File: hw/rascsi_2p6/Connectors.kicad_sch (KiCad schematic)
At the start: 3 parts, among them J20 171826-4, J3 Conn_02x25_Odd_Even, J9 Conn_02x25_Odd_Even

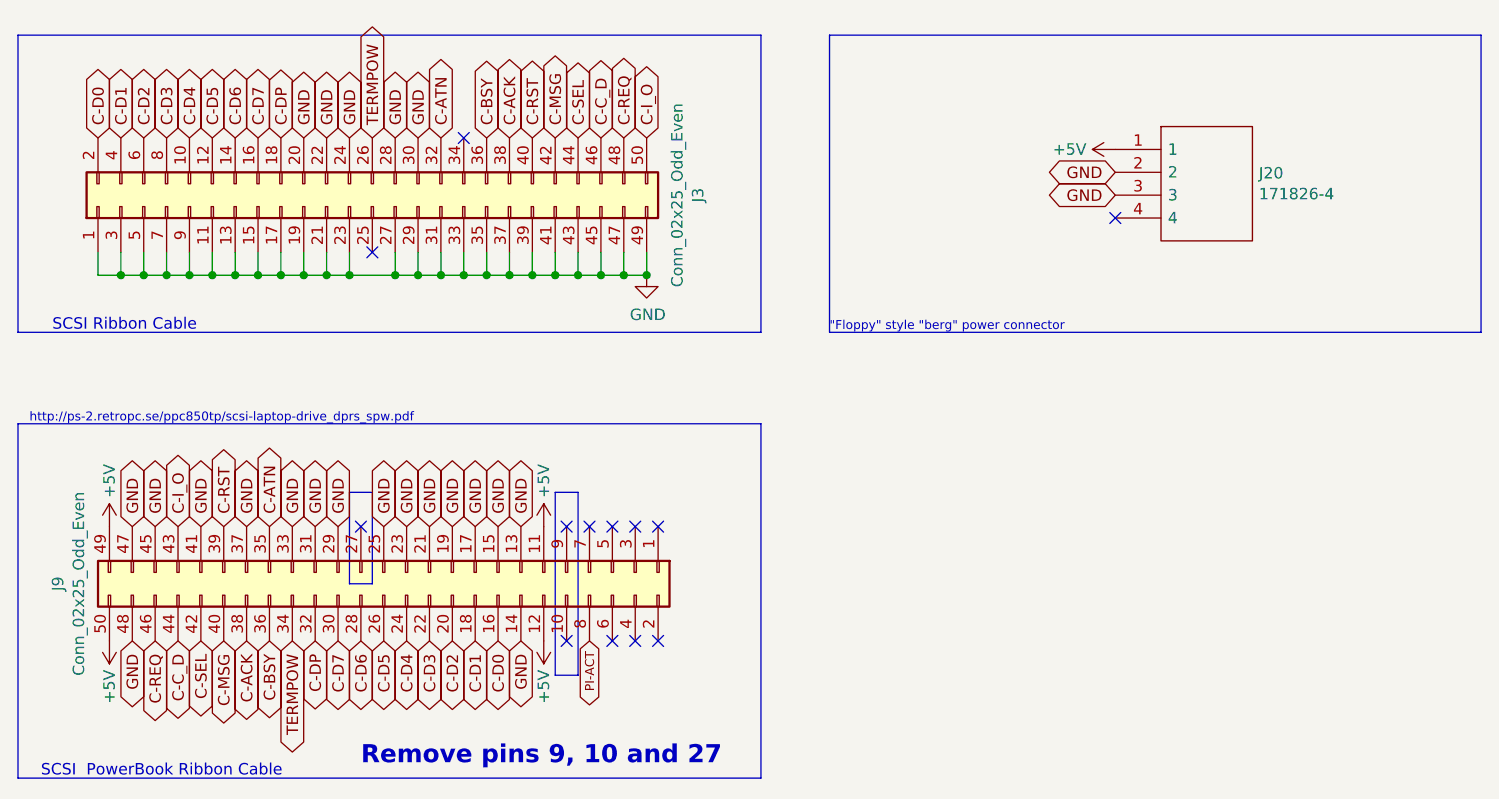
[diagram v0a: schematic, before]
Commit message: Updated with 74LVT245 - as ordered
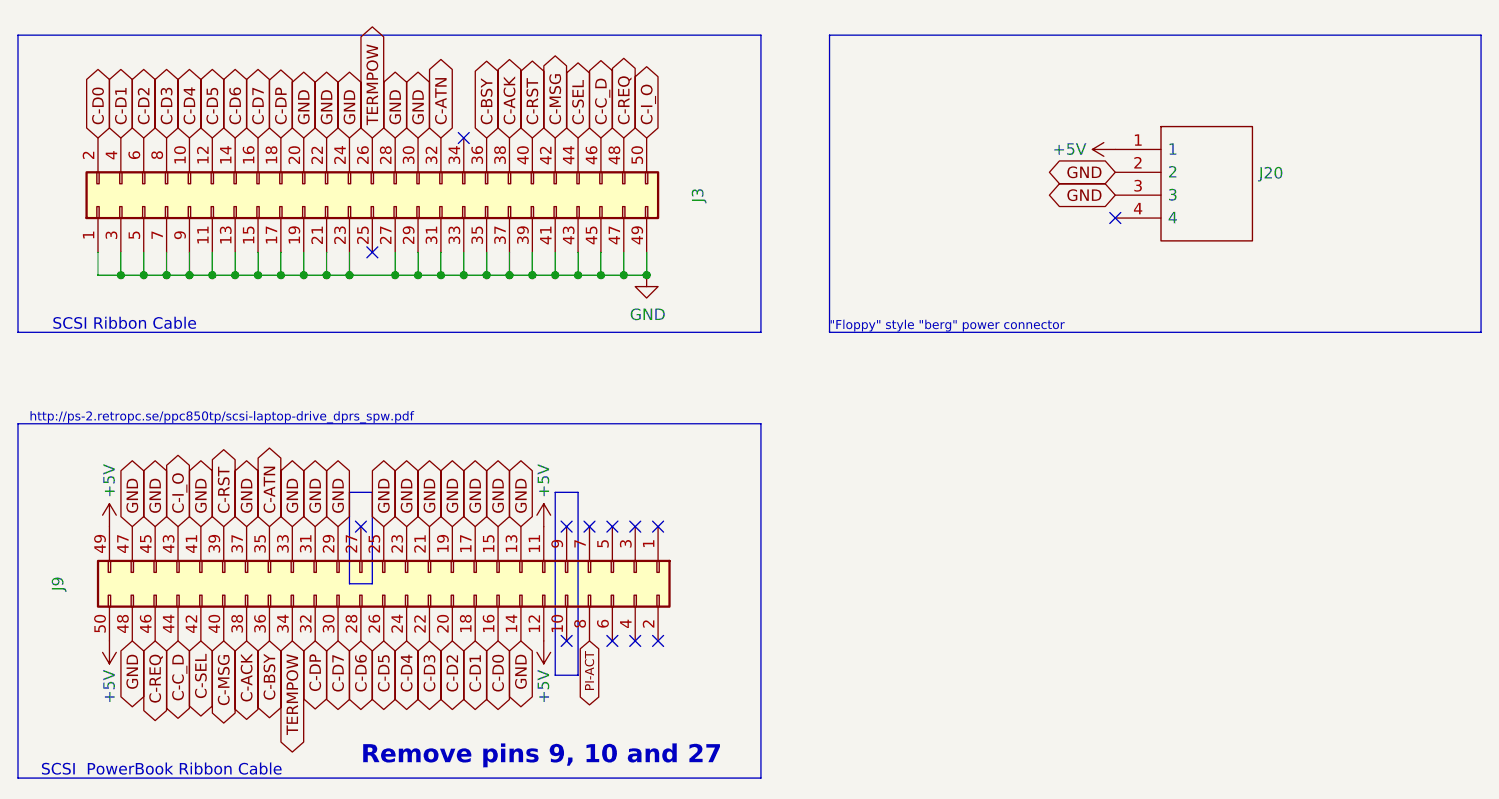
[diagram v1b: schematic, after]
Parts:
- J20: value 171826-4 -> (none); footprint Connector_PinHeader_2.54mm:PinHeader_1x04_P2.54mm_Vertical -> (none)
- J3: value Conn_02x25_Odd_Even -> (none); footprint Connector_PinHeader_2.54mm:PinHeader_2x25_P2.54mm_Vertical -> (none)
- J9: value Conn_02x25_Odd_Even -> (none); footprint Connector_PinHeader_2.00mm:PinHeader_2x25_P2.00mm_Horizontal -> (none)
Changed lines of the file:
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@@
     (in_bom yes) (on_board yes)
     (property "Reference" "J3" (id 0) (at 111.125 41.91 0))
-    (property "Value" "Conn_02x25_Odd_Even" (id 1) (at 108.8136 41.91 0))
-    (property "Footprint" "Connector_PinHeader_2.54mm:PinHeader_2x25_P2.54mm_Vertical" (id 2) (at 74.93 43.18 0)
+    (property "Value" "" (id 1) (at 108.8136 41.91 0))
+    (property "Footprint" "" (id 2) (at 74.93 43.18 0)
       (effects (font (size 1.27 1.27)) hide)
     )
@@
     (in_bom yes) (on_board yes)
     (property "Reference" "J9" (id 0) (at 40.005 85.09 0))
-    (property "Value" "Conn_02x25_Odd_Even" (id 1) (at 42.3164 85.09 0))
-    (property "Footprint" "Connector_PinHeader_2.00mm:PinHeader_2x25_P2.00mm_Horizontal" (id 2) (at 76.2 83.82 0)
+    (property "Value" "" (id 1) (at 42.3164 85.09 0))
+    (property "Footprint" "" (id 2) (at 76.2 83.82 0)
       (effects (font (size 1.27 1.27)) hide)
     )
@@
       (effects (font (size 1.27 1.27)) (justify left))
     )
-    (property "Value" "171826-4" (id 1) (at 173.4312 41.783 0)
+    (property "Value" "" (id 1) (at 173.4312 41.783 0)
       (effects (font (size 1.27 1.27)) (justify left))
     )
-    (property "Footprint" "Connector_PinHeader_2.54mm:PinHeader_1x04_P2.54mm_Vertical" (id 2) (at 173.99 34.29 0)
+    (property "Footprint" "" (id 2) (at 173.99 34.29 0)
       (effects (font (size 1.27 1.27)) (justify left) hide)
     )
